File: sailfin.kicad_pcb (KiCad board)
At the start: 2 copper layers, 96.5 x 93 mm, 187 parts, among them J1 AnalogIn, J19 Barrel_Jack_Switch, J2 ATO1, J3 Raspberry_Pi_2_3, J4 Conn_02x25_Odd_Even, J5 i2c, J6 Screw_Terminal_01x02, J7 1wire, J8 PwmOut, J9 AnalogOut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

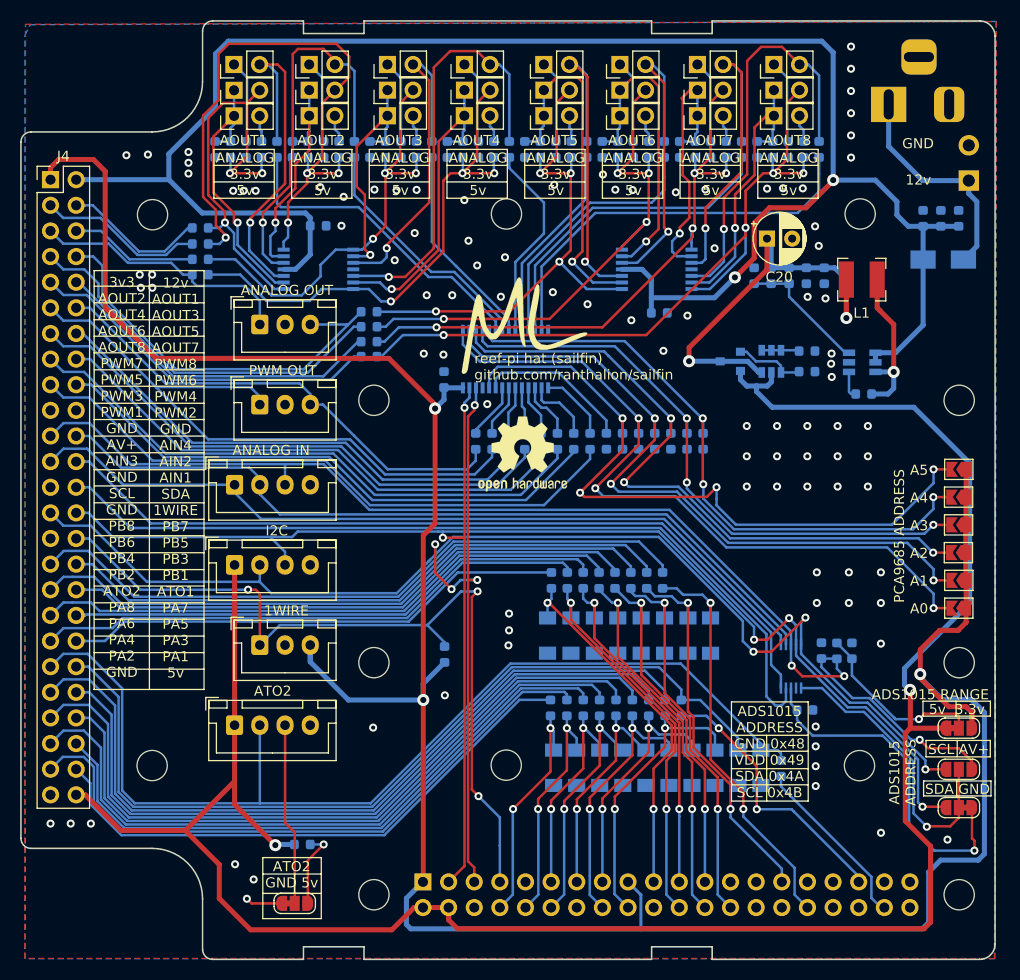
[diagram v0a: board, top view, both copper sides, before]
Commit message: 100mm front panel
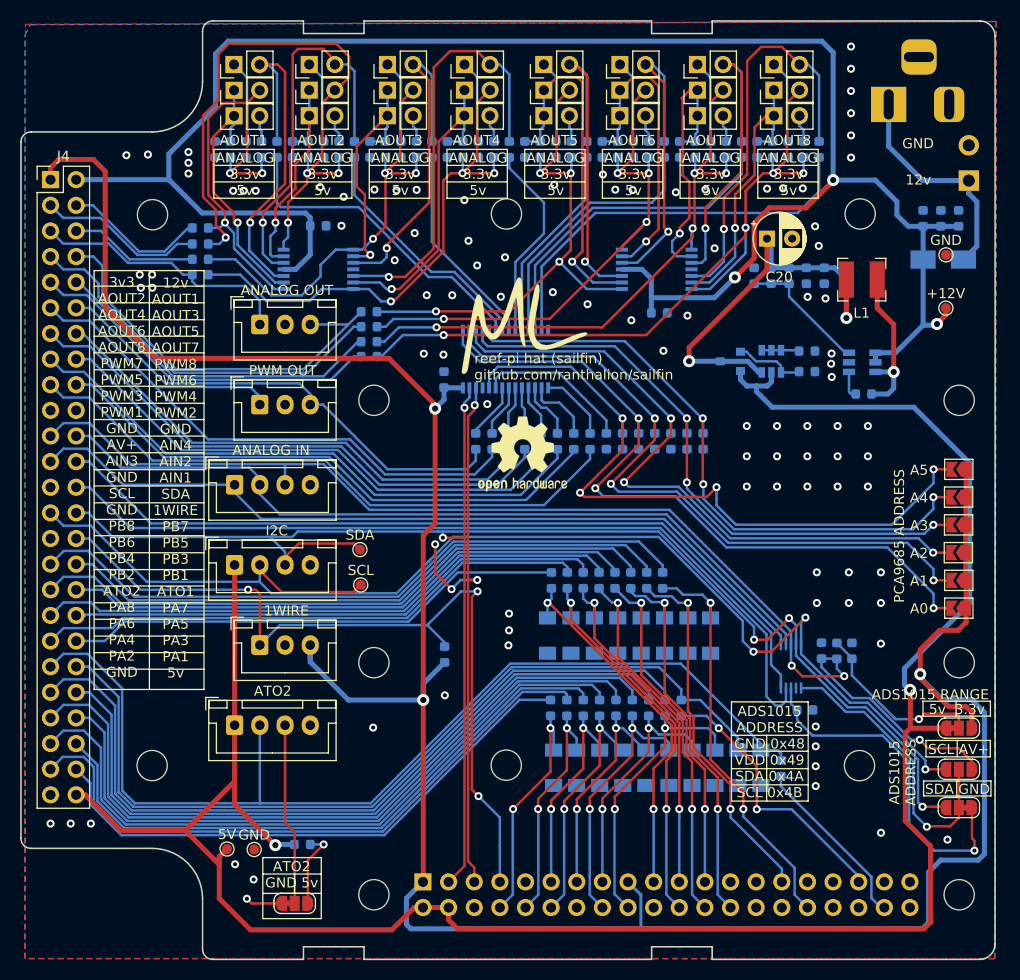
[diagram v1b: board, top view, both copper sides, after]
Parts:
- added +12V: TestPoint_Pad_D1.0mm, TestPoint:TestPoint_Pad_D1.0mm, F.Cu at (107.1, 126.8)
- added 5V: TestPoint_Pad_D1.0mm, TestPoint:TestPoint_Pad_D1.0mm, F.Cu at (35.9, 180.4)
- added GND: TestPoint_Pad_D1.0mm, TestPoint:TestPoint_Pad_D1.0mm, F.Cu at (107.2, 121.5)
- added GND: TestPoint_Pad_D1.0mm, TestPoint:TestPoint_Pad_D1.0mm, F.Cu at (38.6, 180.4)
- added SCL: TestPoint_Pad_D1.0mm, TestPoint:TestPoint_Pad_D1.0mm, F.Cu at (49.1, 154.2)
- added SDA: TestPoint_Pad_D1.0mm, TestPoint:TestPoint_Pad_D1.0mm, F.Cu at (49.1, 150.7)
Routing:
- net /SCL: track 173.4 -> 185.1 mm
- net /SDA: track 161.5 -> 170.5 mm
- net +12V: track 184.2 -> 187.6 mm, vias 2 -> 3
- net +5V: track 216.5 -> 218.4 mm
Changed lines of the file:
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@@
     (thickness 1.2)
     (drawings 211)
-    (tracks 1796)
+    (tracks 1812)
     (zones 0)
-    (modules 187)
+    (modules 193)
     (nets 140)
   )
   (page A4)
   (layers
-    (0 F.Cu signal hide)
+    (0 F.Cu signal)
     (31 B.Cu signal)
     (32 B.Adhes user)
     (33 F.Adhes user)
     (34 B.Paste user)
-    (35 F.Paste user hide)
+    (35 F.Paste user)
     (36 B.SilkS user)
-    (37 F.SilkS user hide)
+    (37 F.SilkS user)
     (38 B.Mask user)
-    (39 F.Mask user hide)
+    (39 F.Mask user)
     (40 Dwgs.User user)
     (41 Cmts.User user)
@@
     (44 Edge.Cuts user)
     (45 Margin user)
-    (46 B.CrtYd user hide)
-    (47 F.CrtYd user hide)
-    (48 B.Fab user hide)
-    (49 F.Fab user hide)
+    (46 B.CrtYd user)
+    (47 F.CrtYd user)
+    (48 B.Fab user)
+    (49 F.Fab user)
   )
   (setup
@@
     (mod_text_size 1 1)
     (mod_text_width 0.1)
-    (pad_size 2.032 2.032)
-    (pad_drill 1.19888)
+    (pad_size 1 1)
+    (pad_drill 0)
     (pad_to_mask_clearance 0.051)
     (solder_mask_min_width 0.25)
     (aux_axis_origin 0 0)
-    (visible_elements 7FF7FFFF)
+    (visible_elements 7FFFFFFF)
     (pcbplotparams
       (layerselection 0x010fc_ffffffff)
@@
     )
   )
+  (module TestPoint:TestPoint_Pad_D1.0mm (layer F.Cu)
+    (at 107.14 126.78)
+    (descr "SMD pad as test Point, diameter 1.0mm")
+    (tags "test point SMD pad")
+    (attr virtual)
+    (fp_text reference +12V (at 0 -1.448) (layer F.SilkS)
+      (effects (font (size 1 1) (thickness 0.15)))
+    )
+    (fp_text value TestPoint_Pad_D1.0mm (at 0 1.55) (layer F.Fab)
+      (effects (font (size 1 1) (thickness 0.15)))
+    )
+    (fp_circle (center 0 0) (end 0 0.7) (layer F.SilkS) (width 0.12))
+    (fp_circle (center 0 0) (end 1 0) (layer F.CrtYd) (width 0.05))
+    (fp_text user %R (at 0 -1.45) (layer F.Fab)
+      (effects (font (size 1 1) (thickness 0.15)))
+    )
+    (pad 1 smd circle (at 0 0) (size 1 1) (layers F.Cu F.Mask)
+      (net 5 +12V))
+  )
+  (module TestPoint:TestPoint_Pad_D1.0mm (layer F.Cu)
+    (at 107.15 121.5)
+    (descr "SMD pad as test Point, diameter 1.0mm")
+    (tags "test point SMD pad")
+    (attr virtual)
+    (fp_text reference GND (at 0 -1.448) (layer F.SilkS)
+      (effects (font (size 1 1) (thickness 0.15)))
+    )
+    (fp_text value TestPoint_Pad_D1.0mm (at 0 1.55) (layer F.Fab)
+      (effects (font (size 1 1) (thickness 0.15)))
+    )
+    (fp_circle (center 0 0) (end 0 0.7) (layer F.SilkS) (width 0.12))
+    (fp_circle (center 0 0) (end 1 0) (layer F.CrtYd) (width 0.05))
+    (fp_text user %R (at 0 -1.45) (layer F.Fab)
+      (effects (font (size 1 1) (thickness 0.15)))
+    )
+    (pad 1 smd circle (at 0 0) (size 1 1) (layers F.Cu F.Mask)
+      (net 2 GND))
+  )
+  (module TestPoint:TestPoint_Pad_D1.0mm (layer F.Cu)
+    (at 35.9 180.38)
+    (descr "SMD pad as test Point, diameter 1.0mm")
+    (tags "test point SMD pad")
+    (attr virtual)
+    (fp_text reference 5V (at 0 -1.448) (layer F.SilkS)
+      (effects (font (size 1 1) (thickness 0.15)))
+    )
+    (fp_text value TestPoint_Pad_D1.0mm (at 0 1.55) (layer F.Fab)
+      (effects (font (size 1 1) (thickness 0.15)))
+    )
+    (fp_circle (center 0 0) (end 0 0.7) (layer F.SilkS) (width 0.12))
+    (fp_circle (center 0 0) (end 1 0) (layer F.CrtYd) (width 0.05))
+    (fp_text user %R (at 0 -1.45) (layer F.Fab)
+      (effects (font (size 1 1) (thickness 0.15)))
+    )
+    (pad 1 smd circle (at 0 0) (size 1 1) (layers F.Cu F.Mask)
+      (net 17 +5V))
+  )
+  (module TestPoint:TestPoint_Pad_D1.0mm (layer F.Cu)
+    (at 38.59 180.43)
+    (descr "SMD pad as test Point, diameter 1.0mm")
+    (tags "test point SMD pad")
+    (attr virtual)
+    (fp_text reference GND (at 0 -1.448) (layer F.SilkS)
+      (effects (font (size 1 1) (thickness 0.15)))
+    )
+    (fp_text value TestPoint_Pad_D1.0mm (at 0 1.55) (layer F.Fab)
+      (effects (font (size 1 1) (thickness 0.15)))
+    )
+    (fp_circle (center 0 0) (end 0 0.7) (layer F.SilkS) (width 0.12))
+    (fp_circle (center 0 0) (end 1 0) (layer F.CrtYd) (width 0.05))
+    (fp_text user %R (at 0 -1.45) (layer F.Fab)
+      (effects (font (size 1 1) (thickness 0.15)))
+    )
+    (pad 1 smd circle (at 0 0) (size 1 1) (layers F.Cu F.Mask)
+      (net 2 GND))
+  )
+  (module TestPoint:TestPoint_Pad_D1.0mm (layer F.Cu)
+    (at 49.07 150.71)
+    (descr "SMD pad as test Point, diameter 1.0mm")
+    (tags "test point SMD pad")
+    (attr virtual)
+    (fp_text reference SDA (at 0 -1.448) (layer F.SilkS)
+      (effects (font (size 1 1) (thickness 0.15)))
+    )
+    (fp_text value TestPoint_Pad_D1.0mm (at 0 1.55) (layer F.Fab)
+      (effects (font (size 1 1) (thickness 0.15)))
+    )
+    (fp_circle (center 0 0) (end 0 0.7) (layer F.SilkS) (width 0.12))
+    (fp_circle (center 0 0) (end 1 0) (layer F.CrtYd) (width 0.05))
+    (fp_text user %R (at 0 -1.45) (layer F.Fab)
+      (effects (font (size 1 1) (thickness 0.15)))
+    )
+    (pad 1 smd circle (at 0 0) (size 1 1) (layers F.Cu F.Mask)
+      (net 18 /SDA))
+  )
+  (module TestPoint:TestPoint_Pad_D1.0mm (layer F.Cu)
+    (at 49.15 154.21)
+    (descr "SMD pad as test Point, diameter 1.0mm")
+    (tags "test point SMD pad")
+    (attr virtual)
+    (fp_text reference SCL (at 0 -1.448) (layer F.SilkS)
+      (effects (font (size 1 1) (thickness 0.15)))
+    )
+    (fp_text value TestPoint_Pad_D1.0mm (at 0 1.55) (layer F.Fab)
+      (effects (font (size 1 1) (thickness 0.15)))
+    )
+    (fp_circle (center 0 0) (end 0 0.7) (layer F.SilkS) (width 0.12))
+    (fp_circle (center 0 0) (end 1 0) (layer F.CrtYd) (width 0.05))
+    (fp_text user %R (at 0 -1.45) (layer F.Fab)
+      (effects (font (size 1 1) (thickness 0.15)))
+    )
+    (pad 1 smd circle (at 0 0) (size 1 1) (layers F.Cu F.Mask)
+      (net 19 /SCL))
+  )
   (gr_text "reef-pi hat (sailfin)\ngithub.com/ranthalion/sailfin" (at 60.4 132.58) (layer F.SilkS)
     (effects (font (size 1 1) (thickness 0.15)) (justify left))
@@
   (segment (start 104.88 128.47) (end 104.88 121.97) (width 0.5) (layer B.Cu) (net 5))
   (segment (start 102.15 131.2) (end 104.88 128.47) (width 0.5) (layer B.Cu) (net 5))
+  (segment (start 106.26 128.35) (end 106.14 128.47) (width 0.5) (layer B.Cu) (net 5))
+  (segment (start 106.14 128.47) (end 104.88 128.47) (width 0.5) (layer B.Cu) (net 5))
+  (via (at 106.26 128.35) (size 1.2) (drill 0.6) (layers F.Cu B.Cu) (net 5))
+  (segment (start 107.14 127.47) (end 106.26 128.35) (width 0.5) (layer F.Cu) (net 5))
+  (segment (start 107.14 126.78) (end 107.14 127.47) (width 0.5) (layer F.Cu) (net 5))
   (segment (start 74.836632 102.634739) (end 74.844739 102.634739) (width 0.25) (layer B.Cu) (net 6) (status 30))
   (segment (start 74.844739 102.634739) (end 76.09 103.88) (width 0.25) (layer B.Cu) (net 6) (status 10))
@@
   (segment (start 103.618 164.638) (end 103.59 164.61) (width 0.5) (layer F.Cu) (net 17))
   (segment (start 103.618 168.402) (end 103.618 164.638) (width 0.5) (layer F.Cu) (net 17))
+  (segment (start 103.56 164.64) (end 103.59 164.61) (width 0.5) (layer F.Cu) (net 17))
+  (segment (start 35.13 181.15) (end 35.9 180.38) (width 0.5) (layer F.Cu) (net 17))
+  (segment (start 35.13 181.91) (end 35.13 181.15) (width 0.5) (layer F.Cu) (net 17))
   (segment (start 59.925 134.676) (end 59.925 135.655) (width 0.25) (layer B.Cu) (net 18))
   (via (at 59.436 136.652) (size 0.8) (drill 0.4) (layers F.Cu B.Cu) (net 18))
@@
   (segment (start 56.84 148.92001) (end 57.29 148.92001) (width 0.25) (layer B.Cu) (net 18))
   (segment (start 57.29 148.92001) (end 78.68001 148.92001) (width 0.25) (layer B.Cu) (net 18))
+  (segment (start 41.65 152.226) (end 41.65 151.46) (width 0.25) (layer F.Cu) (net 18))
+  (segment (start 41.65 151.46) (end 43 150.11) (width 0.25) (layer F.Cu) (net 18))
+  (segment (start 48.47 150.11) (end 49.07 150.71) (width 0.25) (layer F.Cu) (net 18))
+  (segment (start 43 150.11) (end 48.47 150.11) (width 0.25) (layer F.Cu) (net 18))
   (via (at 60.452 136.398) (size 0.8) (drill 0.4) (layers F.Cu B.Cu) (net 19))
   (segment (start 60.575 134.676) (end 60.575 136.275) (width 0.25) (layer B.Cu) (net 19))
@@
   (segment (start 55.885012 151.87) (end 56.51 151.245012) (width 0.25) (layer B.Cu) (net 19))
   (segment (start 56.51 151.245012) (end 58.305012 149.45) (width 0.25) (layer B.Cu) (net 19))
+  (segment (start 39.15 152.226) (end 39.15 152.75) (width 0.25) (layer F.Cu) (net 19))
+  (segment (start 39.15 152.75) (end 41.32 154.92) (width 0.25) (layer F.Cu) (net 19))
+  (segment (start 48.44 154.92) (end 49.15 154.21) (width 0.25) (layer F.Cu) (net 19))
+  (segment (start 41.32 154.92) (end 48.44 154.92) (width 0.25) (layer F.Cu) (net 19))
   (segment (start 62.94 183.64) (end 62.94 180.04) (width 0.25) (layer B.Cu) (net 20))
   (segment (start 62.94 180.04) (end 62.94 180.03) (width 0.25) (layer B.Cu) (net 20))
